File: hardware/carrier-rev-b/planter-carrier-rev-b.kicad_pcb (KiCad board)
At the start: 2 copper layers, 50.1 x 32.6 mm, 24 parts, among them J1 PROTECTED BATTERY, J2 MOISTURE PROBE, J3 WEACT 1.54 INCH, J4 XIAO BAT LEADS, Q1 AO3401A, U1 Seeed XIAO ESP32-C6 or ESP32-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

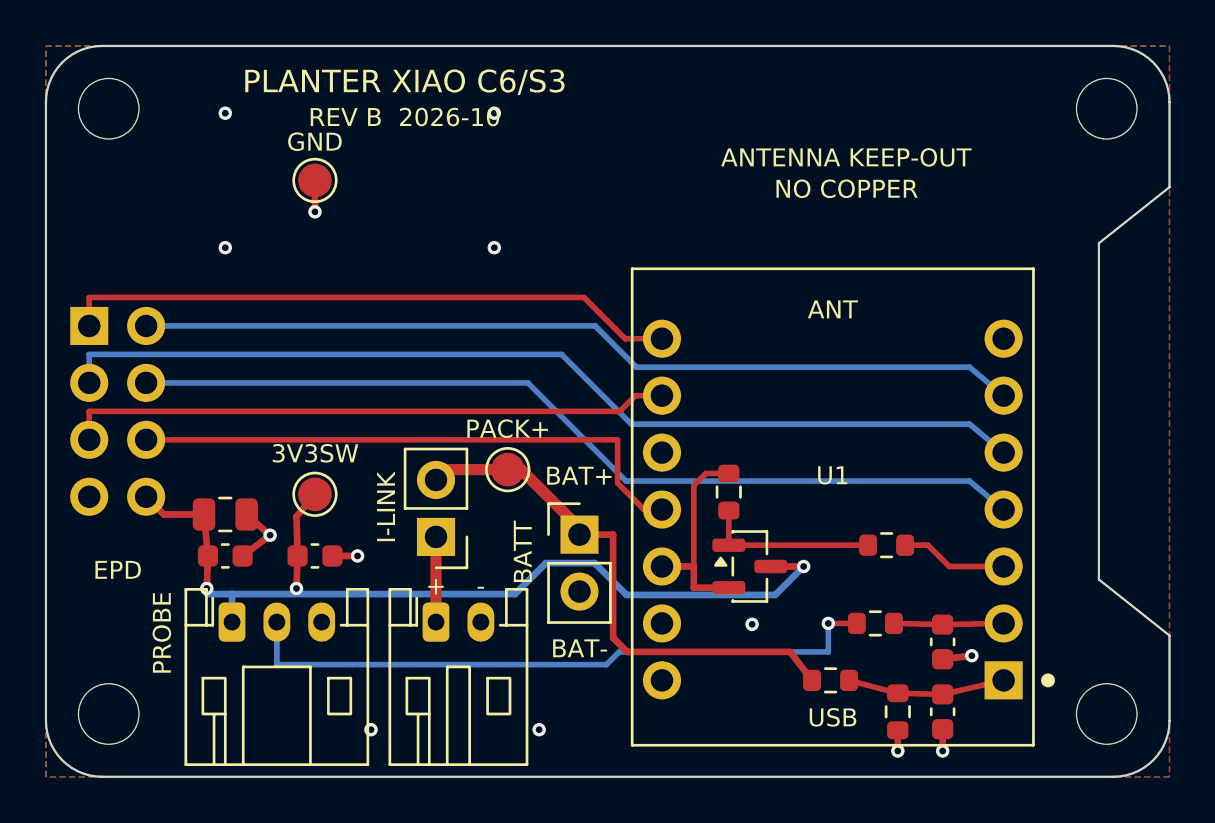
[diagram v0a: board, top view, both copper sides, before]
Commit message: Rev B carrier: add DW01A/FS8205A protection, drop antenna keep-out, JLCPCB-ready fab
- Battery protection on board: DW01A (U2) + FS8205A (Q2), low-side,
  with R6 100R / C6 100nF supply and R7 1k on VM/CS. GND is now the
  protected pack negative; the cell's negative is PACK_IN-. Charging
  stays with the XIAO (USB-C only).
- Antenna keep-out removed: the board uses an external U.FL antenna, so
  the ground pour runs under the whole module. README says how to
  select the U.FL on the C6.
- LCSC part numbers on every machine-placeable part.
- make_fab.sh: JLCPCB BOM with every designator listed in full (no
  ranges), a separate full BOM including the hand-fitted parts, and a
  top-side CPL in JLCPCB's column names, filtered to the BOM's parts.
- Silkscreen raised to JLCPCB's legend minimums (1.0 mm text,
  0.15 mm lines), labels moved clear of each other and the stitching
  vias. Copper, mask, paste, outline and drills are unchanged by this.
- ERC, DRC (including warnings) and schematic parity all clean.

Co-Authored-By: Claude Opus 5.5 <noreply@anthropic.com>
Claude-Session: https://claude.ai/code/session_01AZKEkQvxhWy7uorWE2pBMp
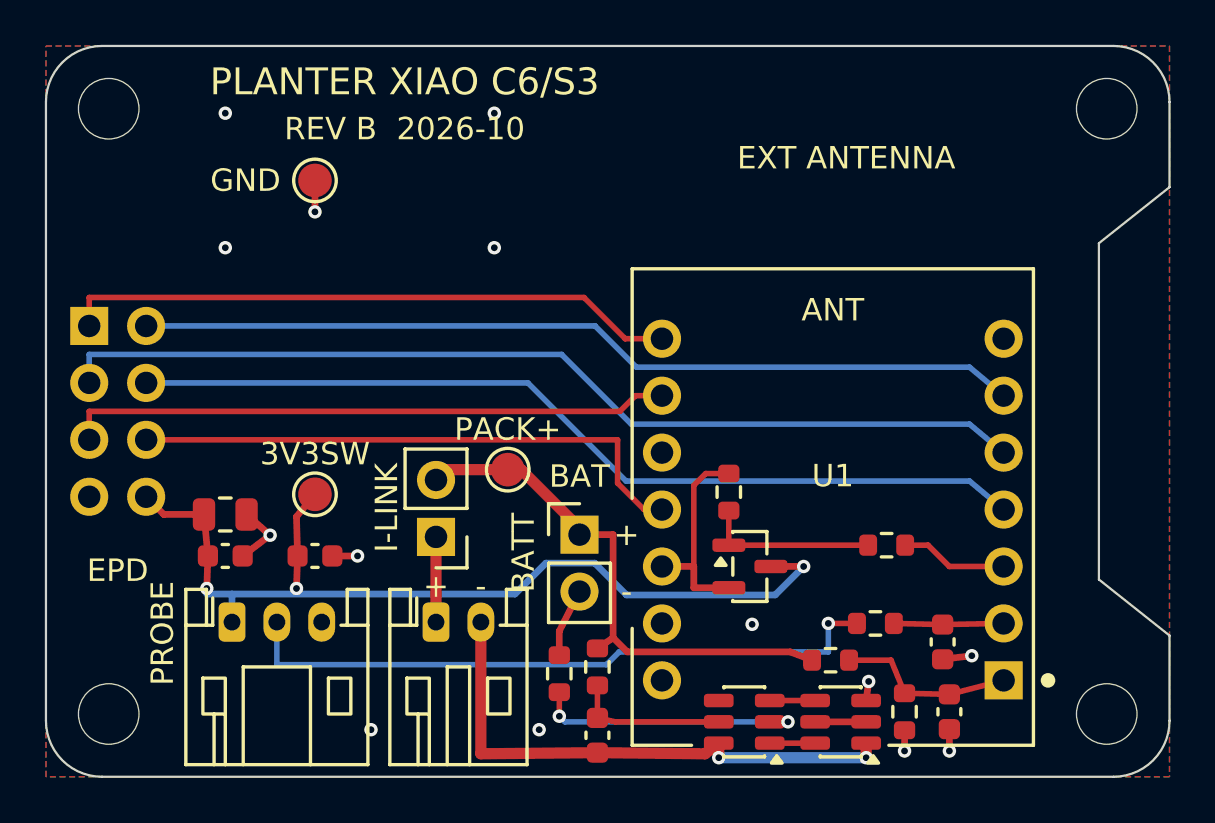
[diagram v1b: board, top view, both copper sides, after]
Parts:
- added C6: 100nF, Capacitor_SMD:C_0603_1608Metric, F.Cu at (124.6, 130.8)
- added Q2: FS8205A, Package_TO_SOT_SMD:SOT-23-6, F.Cu at (135.4, 130.2)
- added R6: 100R, Resistor_SMD:R_0603_1608Metric, F.Cu at (124.6, 127.7)
- added R7: 1k, Resistor_SMD:R_0603_1608Metric, F.Cu at (122.9, 128.0)
- added U2: DW01A, Package_TO_SOT_SMD:SOT-23-6, F.Cu at (131.2, 130.2)
- J1: value PROTECTED BATTERY -> BATTERY CELL
- moved R2 0.90 mm to (135.0, 127.4)
- moved C1 0.30 mm to (140.3, 129.7)
- moved R3 0.30 mm to (138.3, 129.7)
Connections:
- J1 pad 2: /GND -> /PACK_IN-
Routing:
- net /PACK_IN-: track 0.00 -> 24.5 mm, vias 0 -> 2
- net /DW_CS: track 0.00 -> 12.2 mm, vias 0 -> 2
- net /DW_VCC: track 0.00 -> 6.88 mm
- net /GND: track 8.67 -> 12.6 mm, vias 13 -> 14
- net /PROT_D: track 0.00 -> 2.28 mm
- net /DW_OD: track 0.00 -> 2.03 mm
- net /DW_OC: track 0.00 -> 2.03 mm
- net /VBAT_ADC: track 7.04 -> 7.97 mm
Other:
- board text added: "BAT"
- board text added: "EXT ANTENNA"
- board text removed: "ANTENNA KEEP-OUT"
- board text removed: "BAT+"
- board text removed: "BAT-"
- board text removed: "NO COPPER"
